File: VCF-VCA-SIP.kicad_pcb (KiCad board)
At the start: 2 copper layers, 46 x 18 mm, 45 parts, among them P1 CONN_10, Q1 BC857BS, U1 LM13700, U2 TL072-, U3 LM13700, U4 TL072-, U5 LM13700, U6 TL072-

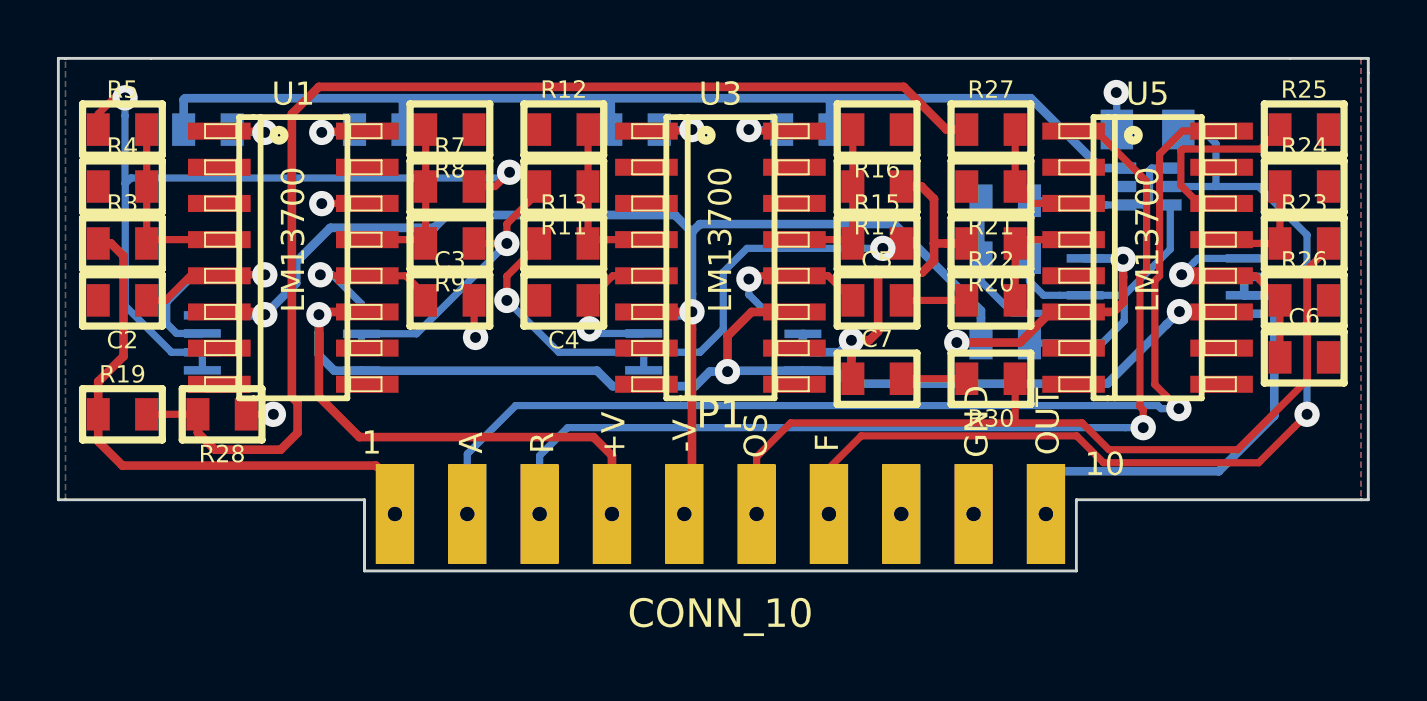
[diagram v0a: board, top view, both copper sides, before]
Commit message: updated from commit 81417c2. Routed
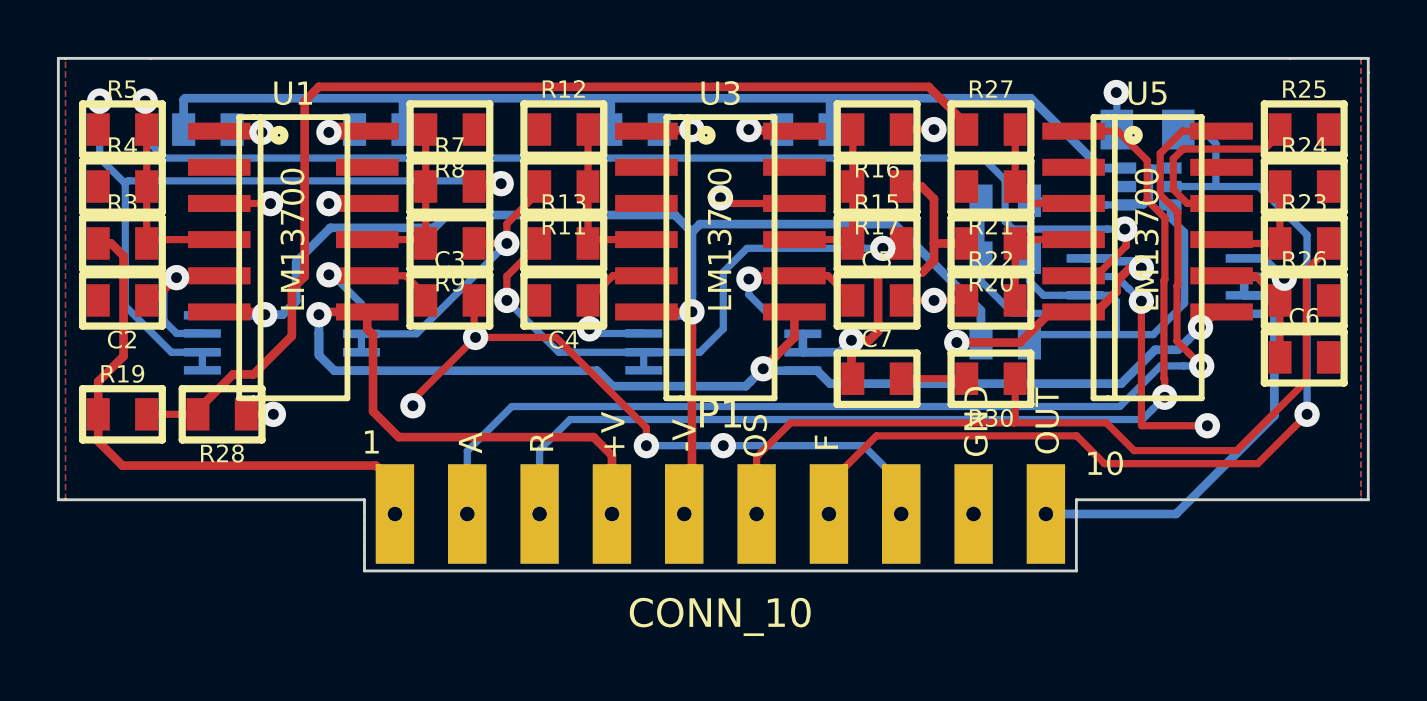
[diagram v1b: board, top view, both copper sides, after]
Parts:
- U1, U3, U5: footprint MyModules:SO16-JRL -> MyModules:SOIC16-12-JRL
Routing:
- net Net-(R3-Pad2): track 6.61 -> 48.5 mm, vias 0 -> 2
- net GND: track 7.48 -> 43.7 mm, vias 4 -> 13
- net Net-(C2-Pad1): track 10.9 -> 6.42 mm
- net Net-(R19-Pad2): track 42.6 -> 38.9 mm
- net +VCC: track 60.6 -> 57.1 mm
- net Net-(C1-Pad2): track 14.1 -> 16.8 mm
- net Net-(R5-Pad1): track 28.1 -> 26.8 mm
- net -VCC: track 57.1 -> 58.1 mm
- net RES_CTRL: track 35.7 -> 36.6 mm
- net VCA_OUT: track 15.9 -> 15.2 mm
- net Net-(C3-Pad1): track 6.44 -> 5.84 mm
- net Net-(R25-Pad1): track 6.69 -> 7.24 mm
- net Net-(C6-Pad1): track 8.26 -> 7.72 mm
- net Net-(R10-Pad1): track 2.81 -> 2.31 mm
